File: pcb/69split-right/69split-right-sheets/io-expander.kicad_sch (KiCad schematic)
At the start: 5 parts, among them U1 MCP23017_SS

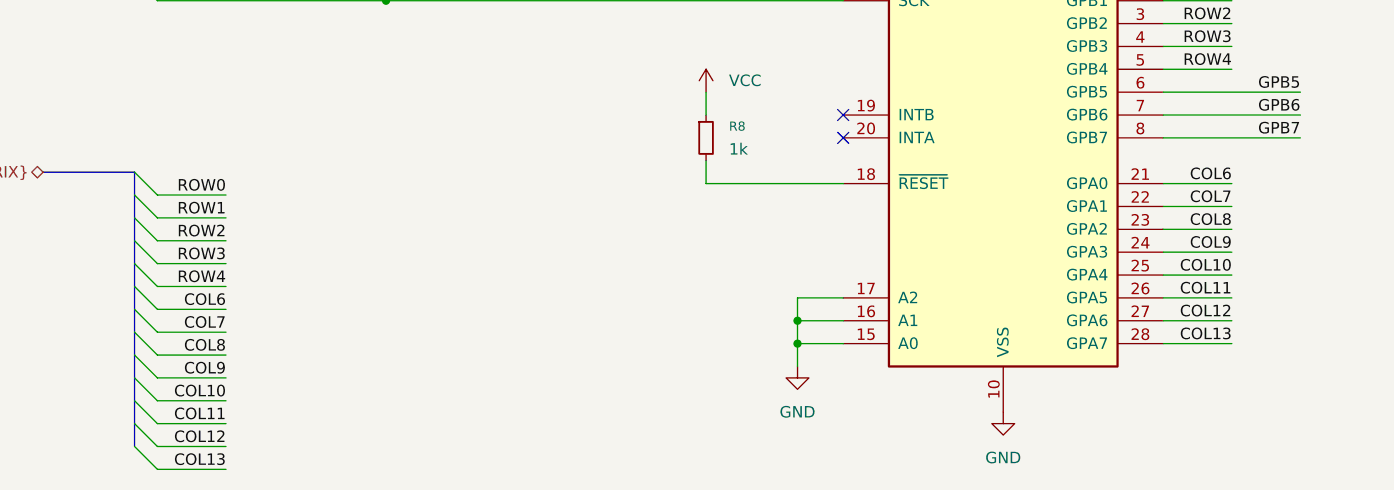
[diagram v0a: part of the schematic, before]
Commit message: Fix column number labels
Before it started from COL6 but it should start from COL7 because COL6
is on the left PCB.
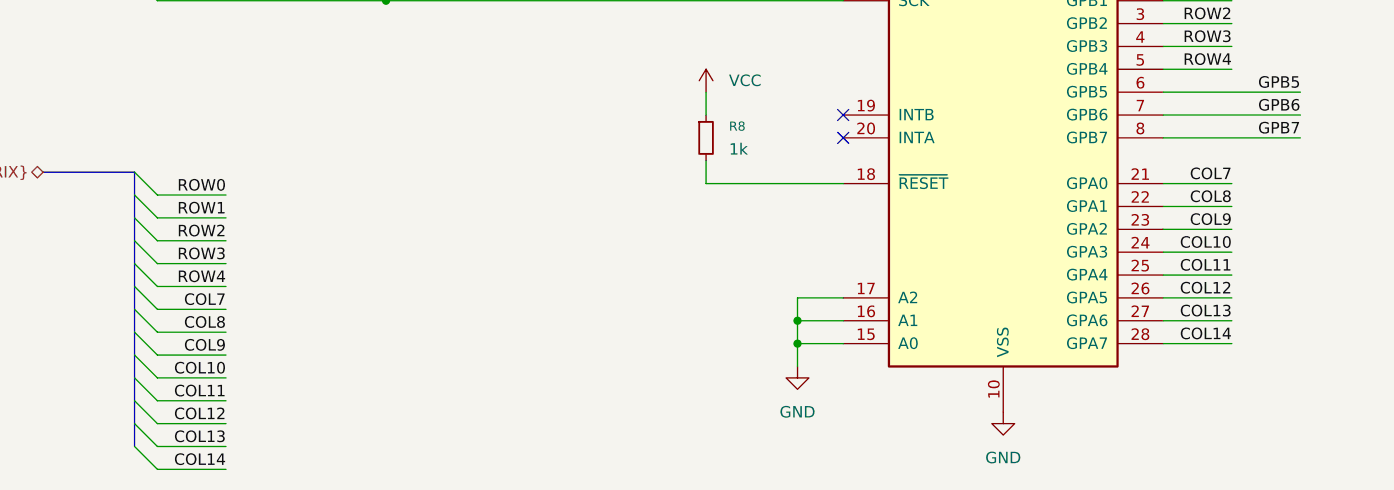
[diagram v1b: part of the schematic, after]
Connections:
- net COL6 is gone; now on net COL7: U1.21 (GPA0)
- net COL10: now also U1.24 (GPA3); no longer U1.25 (GPA4)
- net COL11: now also U1.25 (GPA4); no longer U1.26 (GPA5)
- net COL12: now also U1.26 (GPA5); no longer U1.27 (GPA6)
- net COL13: now also U1.27 (GPA6); no longer U1.28 (GPA7)
- net COL7: no longer U1.22 (GPA1)
- net COL8: now also U1.22 (GPA1); no longer U1.23 (GPA2)
- net COL9: now also U1.23 (GPA2); no longer U1.24 (GPA3)
- new net COL14: U1.28 (GPA7)
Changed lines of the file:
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@@
 		)
 	)
-	(label "COL12"
+	(label "COL13"
 		(at 185.42 121.92 180)
 		(effects
@@
 		)
 	)
-	(label "COL9"
+	(label "COL10"
 		(at 73.66 128.27 180)
 		(effects
@@
 		)
 	)
+	(label "COL8"
+		(at 185.42 109.22 180)
+		(effects
+			(font
+				(size 1.27 1.27)
+			)
+			(justify right bottom)
+		)
+	)
 	(label "COL7"
-		(at 185.42 109.22 180)
-		(effects
-			(font
-				(size 1.27 1.27)
-			)
-			(justify right bottom)
-		)
-	)
-	(label "COL6"
 		(at 185.42 106.68 180)
 		(effects
@@
 		)
 	)
-	(label "COL6"
+	(label "COL7"
 		(at 73.66 120.65 180)
 		(effects
@@
 		)
 	)
-	(label "COL8"
+	(label "COL9"
 		(at 185.42 111.76 180)
 		(effects
@@
 		)
 	)
+	(label "COL10"
+		(at 185.42 114.3 180)
+		(effects
+			(font
+				(size 1.27 1.27)
+			)
+			(justify right bottom)
+		)
+	)
+	(label "COL11"
+		(at 73.66 130.81 180)
+		(effects
+			(font
+				(size 1.27 1.27)
+			)
+			(justify right bottom)
+		)
+	)
 	(label "COL9"
-		(at 185.42 114.3 180)
-		(effects
-			(font
-				(size 1.27 1.27)
-			)
-			(justify right bottom)
-		)
-	)
-	(label "COL10"
-		(at 73.66 130.81 180)
-		(effects
-			(font
-				(size 1.27 1.27)
-			)
-			(justify right bottom)
-		)
-	)
-	(label "COL8"
 		(at 73.66 125.73 180)
 		(effects
@@
 		)
 	)
-	(label "COL13"
+	(label "COL14"
 		(at 185.42 124.46 180)
 		(effects
@@
 		)
 	)
+	(label "COL12"
+		(at 73.66 133.35 180)
+		(effects
+			(font
+				(size 1.27 1.27)
+			)
+			(justify right bottom)
+		)
+	)
 	(label "COL11"
-		(at 73.66 133.35 180)
-		(effects
-			(font
-				(size 1.27 1.27)
-			)
-			(justify right bottom)
-		)
-	)
-	(label "COL10"
 		(at 185.42 116.84 180)
 		(effects
@@
 		)
 	)
-	(label "COL12"
+	(label "COL13"
 		(at 73.66 135.89 180)
 		(effects
@@
 		)
 	)
-	(label "COL13"
+	(label "COL14"
 		(at 73.66 138.43 180)
 		(effects
@@
 		)
 	)
-	(label "COL7"
+	(label "COL8"
 		(at 73.66 123.19 180)
 		(effects
@@
 		)
 	)
-	(label "COL11"
+	(label "COL12"
 		(at 185.42 119.38 180)
 		(effects
